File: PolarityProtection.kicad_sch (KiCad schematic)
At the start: 5 parts, among them Q101 BSC010N04LS, U101 LM74502-Q1

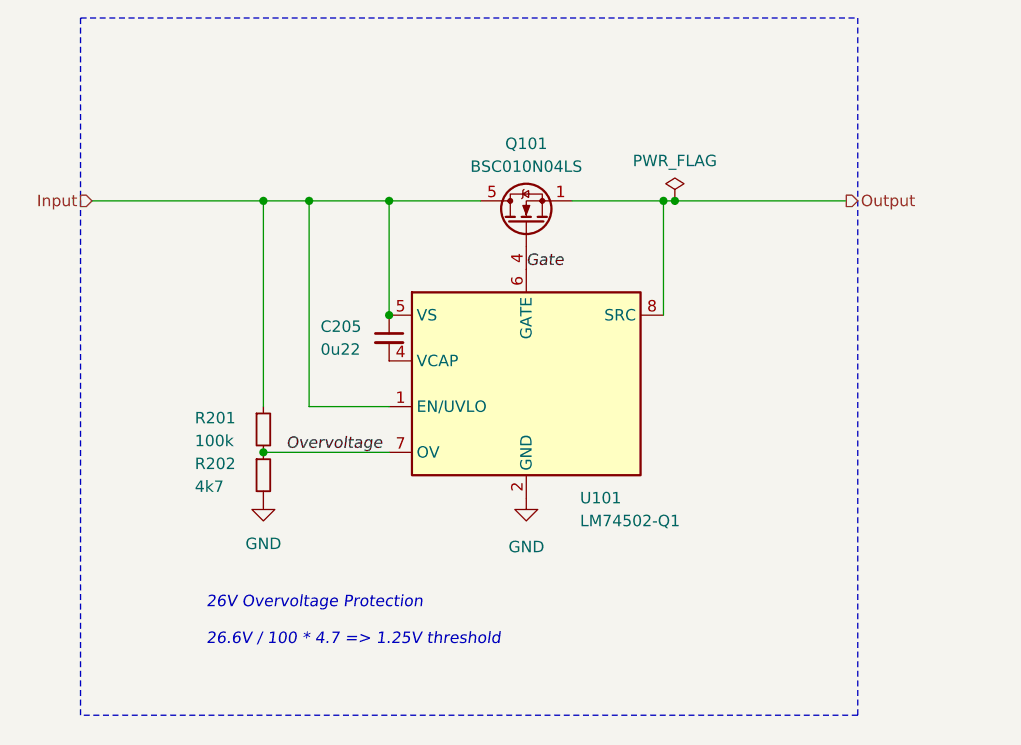
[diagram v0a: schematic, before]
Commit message: Update to Kicad 8
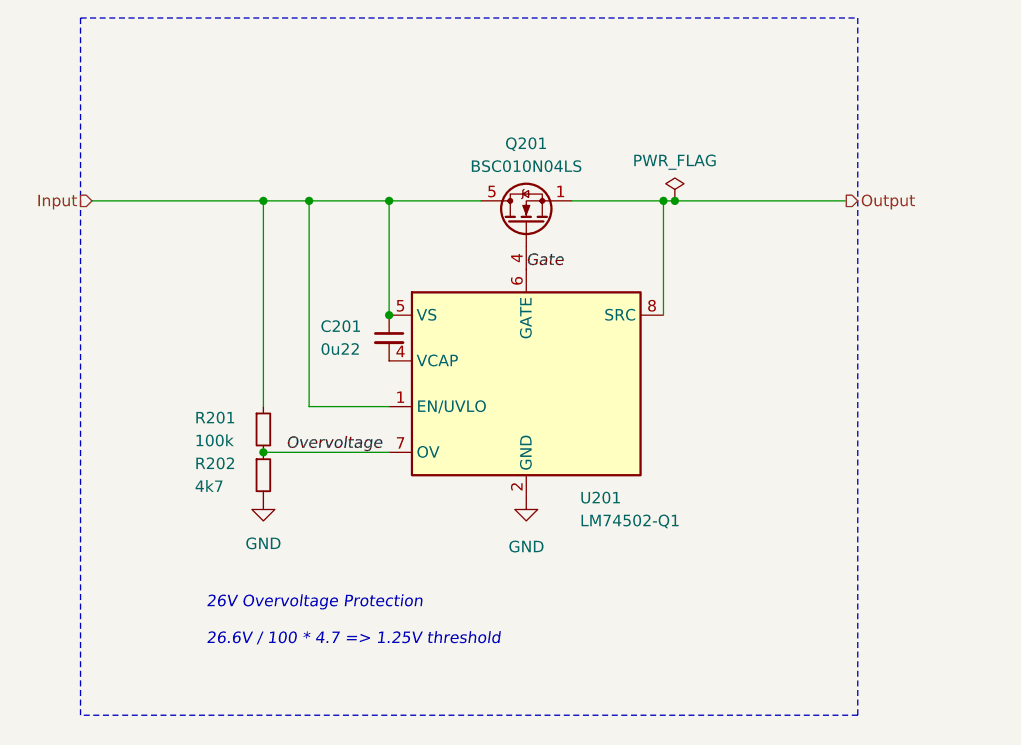
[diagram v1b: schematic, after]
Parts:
- renumbered C205 to C201, Q101 to Q201, U101 to U201

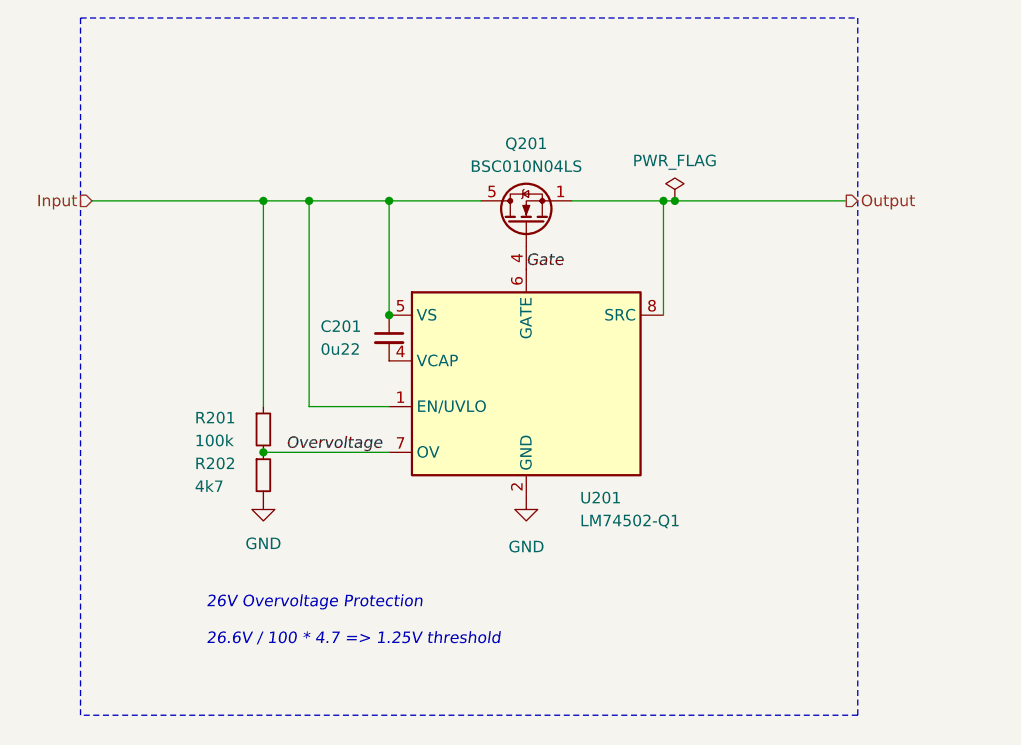
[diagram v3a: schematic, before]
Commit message: Back-to-back Mosfet
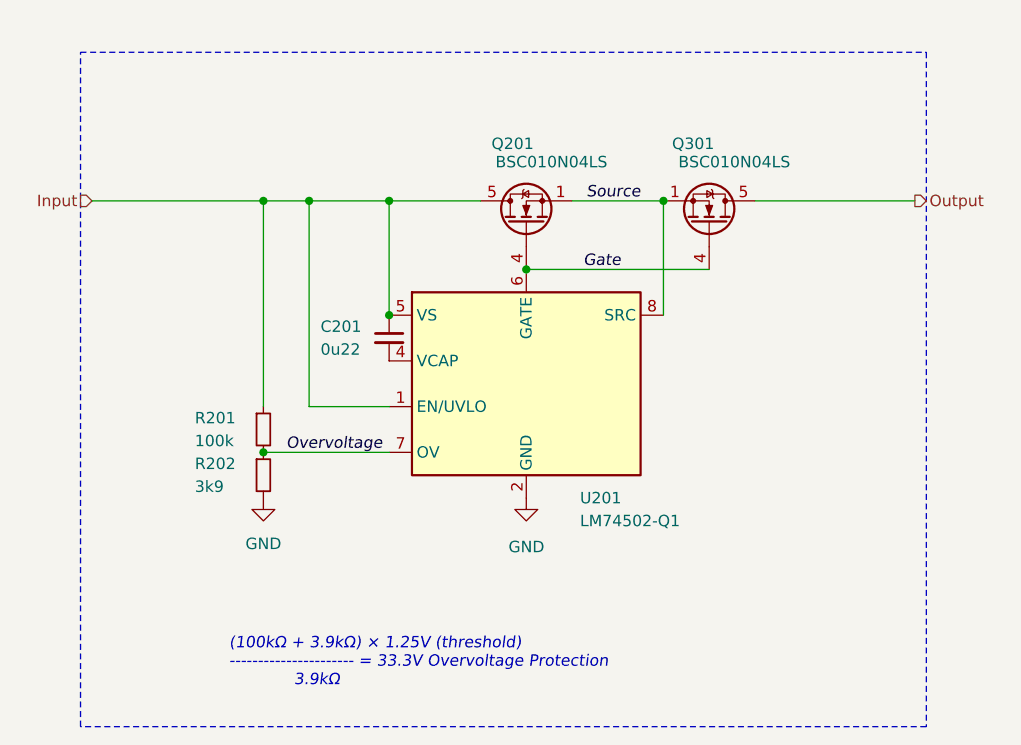
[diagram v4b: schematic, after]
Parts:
- added Q301: BSC010N04LS, V2_Package_TO_SOT_SMD:TDSON-8-FL, symbol V2_Transistor_FET:BSC010N04LS
- R202: value 4k7 -> 3k9
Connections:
- net Gate: now also Q301.4 (G)
- net Output: now also Q301.5 (D); no longer Q201.1 (S), U201.8 (SRC)
- new net Source: Q201.1 (S), Q301.1 (S), U201.8 (SRC)
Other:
- note added: "(100kΩ + 3.9kΩ) × 1.25V (threshold) ---------------------- = 33.3V Overvoltage Protection 3.9kΩ"
- note removed: "26V Overvoltage Protection 26.6V / 100 * 4.7 => 1.25V threshold"
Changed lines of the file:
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@@
 (kicad_sch
-	(version 20231120)
+	(version 20250114)
 	(generator "eeschema")
-	(generator_version "8.0")
+	(generator_version "9.0")
 	(paper "A4")
 	(title_block
 		(title "Polarity Protection")
-		(date "2023-08-08")
-		(rev "2")
+		(date "2025-10-24")
+		(rev "3")
 		(company "Versio Duo")
+	)
+	(rectangle
+		(start 101.6 69.85)
+		(end 195.58 144.78)
+		(stroke
+			(width 0)
+			(type dash)
+		)
+		(fill
+			(type none)
+		)
+	)
+	(text "(100kΩ + 3.9kΩ) × 1.25V (threshold)\n---------------------- = 33.3V Overvoltage Protection\n             3.9kΩ"
+		(exclude_from_sim no)
+		(at 118.11 140.462 0)
+		(effects
+			(font
+				(size 1.27 1.27)
+				(italic yes)
+			)
+			(justify left bottom)
+		)
 	)
 	(junction
@@
 	)
 	(junction
-		(at 167.64 86.36)
+		(at 135.89 99.06)
 		(diameter 0)
 		(color 0 0 0 0)
 	)
 	(junction
-		(at 135.89 99.06)
+		(at 151.13 93.98)
 		(diameter 0)
 		(color 0 0 0 0)
@@
 	(wire
 		(pts
-			(xy 167.64 86.36) (xy 186.69 86.36)
+			(xy 156.21 86.36) (xy 166.37 86.36)
 		)
 		(stroke
@@
 	(wire
 		(pts
+			(xy 176.53 86.36) (xy 194.31 86.36)
+		)
+		(stroke
+			(width 0)
+			(type default)
+		)
+	)
+	(wire
+		(pts
 			(xy 127 86.36) (xy 135.89 86.36)
 		)
@@
 	(wire
 		(pts
+			(xy 151.13 93.98) (xy 171.45 93.98)
+		)
+		(stroke
+			(width 0)
+			(type default)
+		)
+	)
+	(wire
+		(pts
 			(xy 121.92 114.3) (xy 135.89 114.3)
 		)
@@
 	(wire
 		(pts
-			(xy 156.21 86.36) (xy 166.37 86.36)
+			(xy 166.37 86.36) (xy 166.37 99.06)
 		)
 		(stroke
@@
 	(wire
 		(pts
-			(xy 166.37 86.36) (xy 167.64 86.36)
-		)
-		(stroke
-			(width 0)
-			(type default)
-		)
-	)
-	(wire
-		(pts
-			(xy 166.37 86.36) (xy 166.37 99.06)
-		)
-		(stroke
-			(width 0)
-			(type default)
-		)
-	)
-	(wire
-		(pts
 			(xy 127 109.22) (xy 127 86.36)
 		)
@@
 		)
 	)
-	(rectangle
-		(start 101.6 66.04)
-		(end 187.96 143.51)
-		(stroke
-			(width 0)
-			(type dash)
-		)
-		(fill
-			(type none)
-		)
-	)
-	(text "26V Overvoltage Protection\n\n26.6V / 100 * 4.7 => 1.25V threshold"
-		(exclude_from_sim no)
-		(at 115.57 135.89 0)
+	(label "Gate"
+		(at 157.48 93.98 0)
 		(effects
 			(font
@@
 		)
 	)
-	(label "Gate"
-		(at 151.13 93.98 0)
-		(fields_autoplaced yes)
+	(label "Overvoltage"
+		(at 124.46 114.3 0)
 		(effects
 			(font
@@
 		)
 	)
-	(label "Overvoltage"
-		(at 124.46 114.3 0)
-		(fields_autoplaced yes)
+	(label "Source"
+		(at 163.83 86.36 180)
 		(effects
 			(font
@@
 				(italic yes)
 			)
-			(justify left bottom)
+			(justify right bottom)
 		)
 	)
@@
 		(shape input)
 		(at 102.87 86.36 180)
-		(fields_autoplaced yes)
 		(effects
 			(font
@@
 	(hierarchical_label "Output"
 		(shape output)
-		(at 186.69 86.36 0)
-		(fields_autoplaced yes)
+		(at 194.31 86.36 0)
 		(effects
 			(font
@@
 		(on_board yes)
 		(dnp no)
-		(fields_autoplaced yes)
 		(property "Reference" "Q201"
-			(at 151.13 80.01 90)
+			(at 149.606 80.01 90)
 			(effects
 				(font
@@
 		)
 		(property "Value" "BSC010N04LS"
-			(at 151.13 82.55 90)
+			(at 153.924 82.042 90)
 			(effects
 				(font
@@
 				(path "/6c8448b4-b04d-47e1-934e-e40cbe27a7be/e1a18e88-9abf-461b-8346-1c1c4b1e9326"
 					(reference "Q201")
-					(unit 1)
-				)
-			)
-		)
-	)
-	(symbol
-		(lib_id "power:PWR_FLAG")
-		(at 167.64 86.36 0)
-		(unit 1)
-		(exclude_from_sim no)
-		(in_bom yes)
-		(on_board yes)
-		(dnp no)
-		(property "Reference" "#FLG0201"
-			(at 167.64 84.455 0)
-			(effects
-				(font
-					(size 1.27 1.27)
-				)
-				(hide yes)
-			)
-		)
-		(property "Value" "PWR_FLAG"
-			(at 167.64 81.915 0)
-			(effects
-				(font
-					(size 1.27 1.27)
-				)
-			)
-		)
-		(property "Footprint" ""
-			(at 167.64 86.36 0)
-			(effects
-				(font
-					(size 1.27 1.27)
-				)
-				(hide yes)
-			)
-		)
-		(property "Datasheet" "~"
-			(at 167.64 86.36 0)
-			(effects
-				(font
-					(size 1.27 1.27)
-				)
-				(hide yes)
-			)
-		)
-		(property "Description" "Special symbol for telling ERC where power comes from"
-			(at 167.64 86.36 0)
-			(effects
-				(font
-					(size 1.27 1.27)
-				)
-				(hide yes)
-			)
-		)
-		(pin "1"
-		)
-		(instances
-			(project "power-rj45"
-				(path "/6c8448b4-b04d-47e1-934e-e40cbe27a7be/e1a18e88-9abf-461b-8346-1c1c4b1e9326"
-					(reference "#FLG0201")
 					(unit 1)
 				)
@@
 			)
 		)
-		(property "Value" "4k7"
+		(property "Value" "3k9"
 			(at 114.3 118.11 0)
 			(effects
@@
 					(unit 1)
 				)
+			)
+		)
+	)
+	(symbol
+		(lib_id "V2_Transistor_FET:BSC010N04LS")
+		(at 171.45 88.9 270)
+		(mirror x)
+		(unit 1)
+		(exclude_from_sim no)
+		(in_bom yes)
+		(on_board yes)
+		(dnp no)
+		(property "Reference" "Q301"
+			(at 169.672 80.01 90)
+			(effects
+				(font
+					(size 1.27 1.27)
+				)
+			)
+		)
+		(property "Value" "BSC010N04LS"
+			(at 174.244 82.042 90)
+			(effects
+				(font
+					(size 1.27 1.27)
+				)
+			)
+		)
+		(property "Footprint" "V2_Package_TO_SOT_SMD:TDSON-8-FL"
+			(at 169.545 83.82 0)
+			(effects
+				(font
+					(size 1.27 1.27)
+				)
+				(justify left)
+				(hide yes)
+			)
+		)
+		(property "Datasheet" ""
+			(at 171.45 88.9 90)
+			(effects
+				(font
+					(size 1.27 1.27)
+				)
+				(justify left)
+				(hide yes)
+			)
+		)
+		(property "Description" ""
+			(at 171.45 88.9 0)
+			(effects
+				(font
+					(size 1.27 1.27)
+				)
+				(hide yes)
+			)
+		)
+		(pin "1"
+		)
+		(pin "4"
+		)
+		(pin "5"
+		)
+		(instances
+			(project "connector-poe"
+				(path "/6c8448b4-b04d-47e1-934e-e40cbe27a7be/e1a18e88-9abf-461b-8346-1c1c4b1e9326"
+					(reference "Q301")
+					(unit 1)
+				)

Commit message: Resize to 70 mm
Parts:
- renumbered C201 to C301, Q201 to Q301, Q301 to Q302, R201 to R301, R202 to R302, U201 to U301
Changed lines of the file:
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@@
 		(on_board yes)
 		(dnp no)
-		(property "Reference" "Q201"
+		(property "Reference" "Q301"
 			(at 149.606 80.01 90)
 			(effects
@@
 			(project "power-rj45"
 				(path "/6c8448b4-b04d-47e1-934e-e40cbe27a7be/e1a18e88-9abf-461b-8346-1c1c4b1e9326"
-					(reference "Q201")
+					(reference "Q301")
 					(unit 1)
 				)
@@
 		(on_board yes)
 		(dnp no)
-		(property "Reference" "U201"
+		(property "Reference" "U301"
 			(at 157.0944 119.38 0)
 			(effects
@@
 			(project "power-rj45"
 				(path "/6c8448b4-b04d-47e1-934e-e40cbe27a7be/e1a18e88-9abf-461b-8346-1c1c4b1e9326"
-					(reference "U201")
+					(reference "U301")
 					(unit 1)
 				)
@@
 		(on_board yes)
 		(dnp no)
-		(property "Reference" "R201"
+		(property "Reference" "R301"
 			(at 114.3 110.49 0)
 			(effects
@@
 			(project "power-rj45"
 				(path "/6c8448b4-b04d-47e1-934e-e40cbe27a7be/e1a18e88-9abf-461b-8346-1c1c4b1e9326"
-					(reference "R201")
+					(reference "R301")
 					(unit 1)
 				)
@@
 		(on_board yes)
 		(dnp no)
-		(property "Reference" "C201"
+		(property "Reference" "C301"
 			(at 128.27 100.33 0)
 			(effects
@@
 			(project "power-rj45"
 				(path "/6c8448b4-b04d-47e1-934e-e40cbe27a7be/e1a18e88-9abf-461b-8346-1c1c4b1e9326"
-					(reference "C201")
+					(reference "C301")
 					(unit 1)
 				)
@@
 		(on_board yes)
 		(dnp no)
-		(property "Reference" "R202"
+		(property "Reference" "R302"
 			(at 114.3 115.57 0)
 			(effects
@@
 			(project "power-rj45"
 				(path "/6c8448b4-b04d-47e1-934e-e40cbe27a7be/e1a18e88-9abf-461b-8346-1c1c4b1e9326"
-					(reference "R202")
+					(reference "R302")
 					(unit 1)
 				)
@@
 		(on_board yes)
 		(dnp no)
-		(property "Reference" "Q301"
+		(property "Reference" "Q302"
 			(at 169.672 80.01 90)
 			(effects
@@
 			(project "connector-poe"
 				(path "/6c8448b4-b04d-47e1-934e-e40cbe27a7be/e1a18e88-9abf-461b-8346-1c1c4b1e9326"
-					(reference "Q301")
+					(reference "Q302")
 					(unit 1)
 				)
@@
 		(on_board yes)
 		(dnp no)
-		(property "Reference" "#PWR0202"
+		(property "Reference" "#PWR0302"
 			(at 151.13 125.73 0)
 			(effects
@@
 			(project "power-rj45"
 				(path "/6c8448b4-b04d-47e1-934e-e40cbe27a7be/e1a18e88-9abf-461b-8346-1c1c4b1e9326"
-					(reference "#PWR0202")
+					(reference "#PWR0302")
 					(unit 1)
 				)
@@
 		(on_board yes)
 		(dnp no)
-		(property "Reference" "#PWR0201"
+		(property "Reference" "#PWR0301"
 			(at 121.92 125.73 0)
 			(effects
@@
 			(project "power-rj45"
 				(path "/6c8448b4-b04d-47e1-934e-e40cbe27a7be/e1a18e88-9abf-461b-8346-1c1c4b1e9326"
-					(reference "#PWR0201")
-					(unit 1)
-				)
+					(reference "#PWR0301")
+					(unit 1)
+				)

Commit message: GND label
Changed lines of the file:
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@@
 				)
 				(justify left)
+				(hide yes)
 			)
 		)
@@
 					(size 1.27 1.27)
 				)
+				(hide yes)
 			)
 		)
